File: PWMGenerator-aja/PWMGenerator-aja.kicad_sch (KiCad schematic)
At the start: 30 parts, among them J1 Conn_01x03_Pin, Q1 2N3904, Q2 2N3904, Q3 2N3906, Q4 2N3906, SW1 SW_SPST, U1 LM7805_TO220, U2 LM339

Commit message: meh
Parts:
- #PWR01: footprint (none) -> Connector_BarrelJack:BarrelJack_SwitchcraftConxall_RAPC10U_Horizontal; symbol Connector:Barrel_Jack -> Connector:Jack-DC
- D6: value LED Green -> LED; footprint LED_THT:LED_D5.0mm_Green -> LED_THT:LED_D5.0mm
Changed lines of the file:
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@@
 				)
 				(justify left)
-				(hide yes)
 			)
 		)
@@
 			)
 		)
-		(property "Value" "LED Green"
+		(property "Value" "LED"
 			(at 127 108.2674 90)
 			(effects
@@
 			)
 		)
-		(property "Footprint" "LED_THT:LED_D5.0mm_Green"
+		(property "Footprint" "LED_THT:LED_D5.0mm"
 			(at 123.19 105.41 0)
 			(effects
@@
 	)
 	(symbol
-		(lib_id "Connector:Barrel_Jack")
+		(lib_id "Connector:Jack-DC")
 		(at 22.86 93.98 0)
 		(unit 1)
@@
 			)
 		)
-		(property "Footprint" ""
+		(property "Footprint" "Connector_BarrelJack:BarrelJack_SwitchcraftConxall_RAPC10U_Horizontal"
 			(at 24.13 94.996 0)
 			(effects

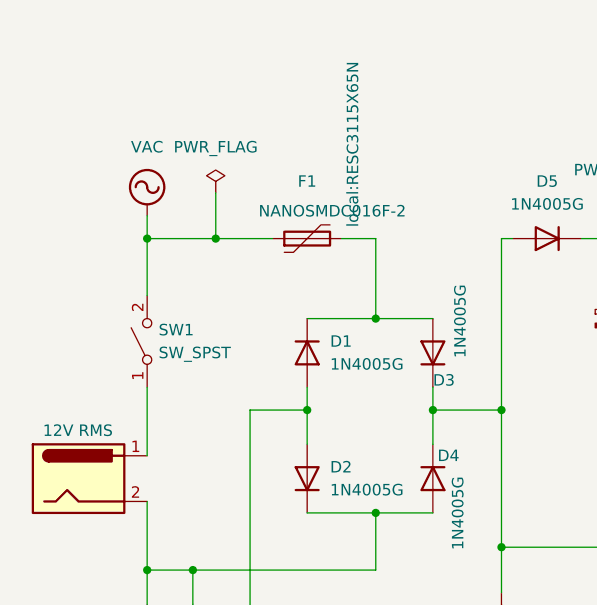
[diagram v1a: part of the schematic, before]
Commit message: Starting component placement
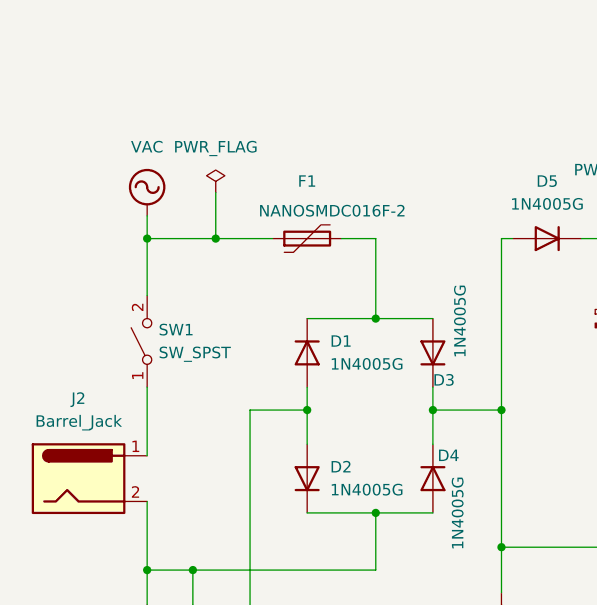
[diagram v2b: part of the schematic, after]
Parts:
- removed #PWR01: 12V RMS, Connector_BarrelJack:BarrelJack_SwitchcraftConxall_RAPC10U_Horizontal, symbol Connector:Jack-DC
- added J2: Barrel_Jack, Connector_BarrelJack:BarrelJack_SwitchcraftConxall_RAPC10U_Horizontal, symbol Connector:Barrel_Jack
- F1: footprint local:RESC3115X65N -> lib:RESC3115X65N
- Q2, Q3, Q4: footprint Package_TO_SOT_THT:TO-92_Inline -> Package_TO_SOT_SMD:SOT-23
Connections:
- net GNDPWR: now also J2.2
- net at SW1.1 (A): now also J2.1
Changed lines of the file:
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@@
 			)
 		)
-		(property "Footprint" "Package_TO_SOT_THT:TO-92_Inline"
+		(property "Footprint" "Package_TO_SOT_SMD:SOT-23"
 			(at 224.79 88.265 0)
 			(effects
@@
 			)
 		)
-		(property "Datasheet" "https://www.onsemi.com/pub/Collateral/2N3903-D.PDF"
+		(property "Datasheet" "https://www.onsemi.com/pub/Collateral/2N3906-D.PDF"
 			(at 219.71 90.17 0)
 			(effects
@@
 	)
 	(symbol
+		(lib_id "Connector:Barrel_Jack")
+		(at 22.86 93.98 0)
+		(unit 1)
+		(exclude_from_sim no)
+		(in_bom yes)
+		(on_board yes)
+		(dnp no)
+		(fields_autoplaced yes)
+		(property "Reference" "J2"
+			(at 22.86 85.09 0)
+			(effects
+				(font
+					(size 1.27 1.27)
+				)
+			)
+		)
+		(property "Value" "Barrel_Jack"
+			(at 22.86 87.63 0)
+			(effects
+				(font
+					(size 1.27 1.27)
+				)
+			)
+		)
+		(property "Footprint" "Connector_BarrelJack:BarrelJack_SwitchcraftConxall_RAPC10U_Horizontal"
+			(at 24.13 94.996 0)
+			(effects
+				(font
+					(size 1.27 1.27)
+				)
+				(hide yes)
+			)
+		)
+		(property "Datasheet" "~"
+			(at 24.13 94.996 0)
+			(effects
+				(font
+					(size 1.27 1.27)
+				)
+				(hide yes)
+			)
+		)
+		(property "Description" "DC Barrel Jack"
+			(at 22.86 93.98 0)
+			(effects
+				(font
+					(size 1.27 1.27)
+				)
+				(hide yes)
+			)
+		)
+		(pin "1"
+		)
+		(pin "2"
+		)
+		(instances
+			(project ""
+				(path "/18199a25-5472-4b5c-b90a-fcfdecd0a2ee"
+					(reference "J2")
+					(unit 1)
+				)
+			)
+		)
+	)
+	(symbol
 		(lib_id "Device:R_US")
 		(at 135.89 76.2 180)
@@
 			)
 		)
-		(property "Footprint" "local:RESC3115X65N"
+		(property "Footprint" "lib:RESC3115X65N"
 			(at 53.34 66.04 0)
 			(effects
@@
 				)
 				(justify left)
+				(hide yes)
 			)
 		)
@@
 	)
 	(symbol
-		(lib_id "Connector:Jack-DC")
-		(at 22.86 93.98 0)
-		(unit 1)
-		(exclude_from_sim no)
-		(in_bom yes)
-		(on_board yes)
-		(dnp no)
-		(property "Reference" "#PWR01"
-			(at 22.86 96.52 0)
-			(effects
-				(font
-					(size 1.27 1.27)
-				)
-				(hide yes)
-			)
-		)
-		(property "Value" "12V RMS"
-			(at 26.67 88.646 0)
-			(effects
-				(font
-					(size 1.27 1.27)
-				)
-				(justify right)
-			)
-		)
-		(property "Footprint" "Connector_BarrelJack:BarrelJack_SwitchcraftConxall_RAPC10U_Horizontal"
-			(at 24.13 94.996 0)
-			(effects
-				(font
-					(size 1.27 1.27)
-				)
-				(hide yes)
-			)
-		)
-		(property "Datasheet" "~"
-			(at 24.13 94.996 0)
-			(effects
-				(font
-					(size 1.27 1.27)
-				)
-				(hide yes)
-			)
-		)
-		(property "Description" "DC Barrel Jack"
-			(at 22.86 93.98 0)
-			(effects
-				(font
-					(size 1.27 1.27)
-				)
-				(hide yes)
-			)
-		)
-		(property "Sim.Pins" "1=+ 2=-"
-			(at 22.86 93.98 0)
-			(effects
-				(font
-					(size 1.27 1.27)
-				)
-				(hide yes)
-			)
-		)
-		(property "Sim.Params" "dc=0 ampl=1 f=1k ac=1"
-			(at 19.05 95.1201 0)
-			(effects
-				(font
-					(size 1.27 1.27)
-				)
-				(justify right)
-				(hide yes)
-			)
-		)
-		(property "Sim.Type" "SIN"
-			(at 22.86 93.98 0)
-			(effects
-				(font
-					(size 1.27 1.27)
-				)
-				(hide yes)
-			)
-		)
-		(property "Sim.Device" "V"
-			(at 22.86 93.98 0)
-			(effects
-				(font
-					(size 1.27 1.27)
-				)
-				(justify left)
-				(hide yes)
-			)
-		)
-		(pin "1"
-		)
-		(pin "2"
-		)
-		(instances
-			(project ""
-				(path "/18199a25-5472-4b5c-b90a-fcfdecd0a2ee"
-					(reference "#PWR01")
-					(unit 1)
-				)
-			)
-		)
-	)
-	(symbol
 		(lib_id "Device:C_Polarized")
 		(at 107.95 76.2 0)
@@
 			)
 		)
-		(property "Footprint" "Package_TO_SOT_THT:TO-92_Inline"
+		(property "Footprint" "Package_TO_SOT_SMD:SOT-23"
 			(at 148.59 107.315 0)
 			(effects
@@
 			)
 		)
-		(property "Datasheet" "https://www.onsemi.com/pub/Collateral/2N3906-D.PDF"
+		(property "Datasheet" "https://www.onsemi.com/pdf/datasheet/pzt3904-d.pdf"
 			(at 143.51 105.41 0)
 			(effects
@@
 			)
 		)
-		(property "Datasheet" "https://www.onsemi.com/pub/Collateral/2N3903-D.PDF"
+		(property "Datasheet" "https://www.onsemi.com/pdf/datasheet/pzt3904-d.pdf"
 			(at 105.41 101.6 0)
 			(effects
@@
 			)
 		)
-		(property "Footprint" "Package_TO_SOT_THT:TO-92_Inline"
+		(property "Footprint" "Package_TO_SOT_SMD:SOT-23"
 			(at 204.47 87.63 0)
 			(effects
@@
 			)
 		)
-		(property "Datasheet" "https://ngspice.sourceforge.io/docs/ngspice-html-manual/manual.xhtml#cha_BJTs"
+		(property "Datasheet" "https://www.onsemi.com/pub/Collateral/2N3906-D.PDF"
 			(at 204.47 87.63 0)
 			(effects
